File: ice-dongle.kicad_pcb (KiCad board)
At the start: 4 copper layers, 40 x 16 mm, 45 parts, among them J1 USB_C_Receptacle_USB2.0, J2 NC Jumper, J3 PROG HEADER, J4 FFC2B35-18-G_REVA2, SW1 SW_Push, SW2 SW_Push, U1 APS6404L-3SQR, U2 W25Q64JWUUIQ, U3 DRTR5V0U4S, U4 MCP1824x-OT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

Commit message: Clean up USB & RGB routing.
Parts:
- moved R7 3.92 mm to (113.7, 109.7), turned to -90 degrees
- moved R9 1.28 mm to (113.3, 107.6)
- moved R8 1.17 mm to (113.3, 111.4)
- moved D2 0.94 mm to (116.2, 110.6), turned to -90 degrees
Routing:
- net /USB_PU: track 15.3 -> 7.96 mm, vias 0 -> 2
- net Net-(D2-Pad3): track 2.50 -> 5.88 mm
- net Net-(D2-Pad2): track 2.75 -> 4.50 mm
- net Net-(J1-PadA7): track 10.4 -> 8.93 mm
- net Net-(J1-PadA6): track 11.7 -> 10.3 mm
- net /USB_DP: track 7.90 -> 6.47 mm
- net /USB_DM: track 7.19 -> 6.09 mm
- net Net-(D2-Pad1): track 3.00 -> 2.47 mm

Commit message: Added
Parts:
- added J5: Qwiic, Connector_PinHeader_1.27mm:PinHeader_1x04_P1.27mm_Vertical, F.Cu at (102.7, 116.1)
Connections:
- U6 pad 3: unconnected-(U6-Pad3) -> Net-(U6-Pad3)
- U6 pad 43: unconnected-(U6-Pad43) -> Net-(U6-Pad43)
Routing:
- net Net-(U6-Pad3): track 0.00 -> 37.1 mm, vias 0 -> 1
- net Net-(U6-Pad43): track 0.00 -> 27.6 mm, vias 0 -> 1
- net /~{BTN}: track 14.5 -> 15.5 mm
- net /PGOOD_1.2: track 23.5 -> 24.0 mm
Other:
- board text added: "Bk"
- board text added: "Bl"
- board text added: "Qwiic"
- board text added: "Rd"
- board text added: "Yl"

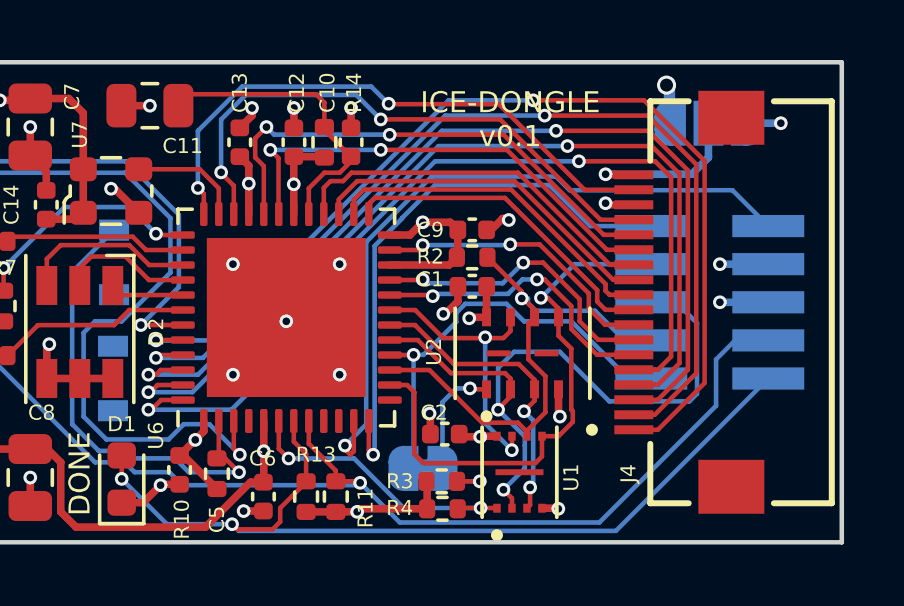
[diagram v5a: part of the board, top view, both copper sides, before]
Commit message: Minor cleanups, add unmarked testpoints to unused IO
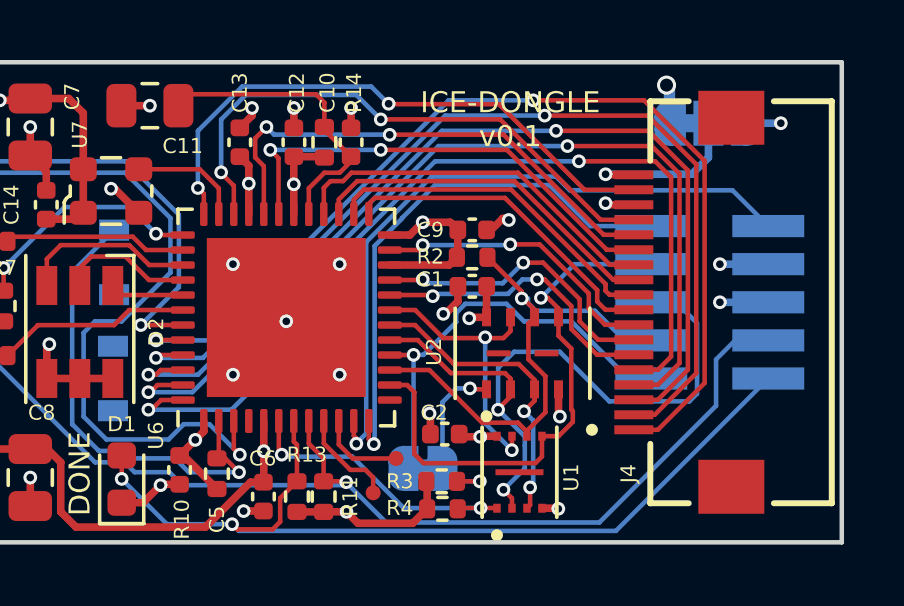
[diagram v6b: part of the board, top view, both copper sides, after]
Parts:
- added TP1: TestPoint, emeb_library:TestPoint_Pad_D0.5mm, F.Cu at (126.0, 116.0)
- added TP2: TestPoint, emeb_library:TestPoint_Pad_D0.5mm, F.Cu at (126.7, 114.8)
- moved R11 0.41 mm to (124.3, 116.1)
- moved R13 0.30 mm to (123.4, 116.1)
- turned JP1 to 0 degrees
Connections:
- JP1 pad 1: +3.3V -> /VUSB
- JP1 pad 3: /VUSB -> +3.3V
- U6 pad 10: unconnected-(U6-Pad10) -> Net-(U6-Pad10)
- U6 pad 9: unconnected-(U6-Pad9) -> Net-(U6-Pad9)
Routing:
- net Net-(U6-Pad9): track 0.00 -> 3.37 mm
- net Net-(U6-Pad10): track 0.00 -> 2.88 mm
- net /SPARE10: track 23.6 -> 22.6 mm
- net /SPARE9: track 18.8 -> 18.1 mm
- net +3.3V: track 33.8 -> 34.4 mm
